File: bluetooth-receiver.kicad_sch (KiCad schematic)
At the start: 12 parts, among them J1 Barrel_Jack_Switch, J2 AudioJack3_Switch, J3 RCJ-22, SW1 PAUSE, SW2 NEXT, SW3 PREV, SW4 ON_OFF, U1 m18, U2 dd1718pa

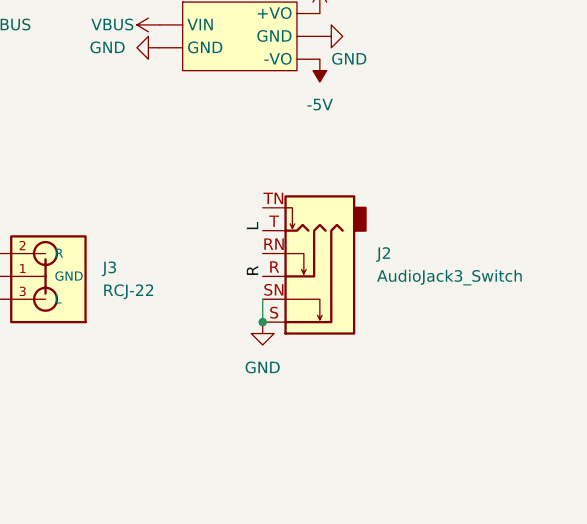
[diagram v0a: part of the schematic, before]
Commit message: Update bluetooth receiver
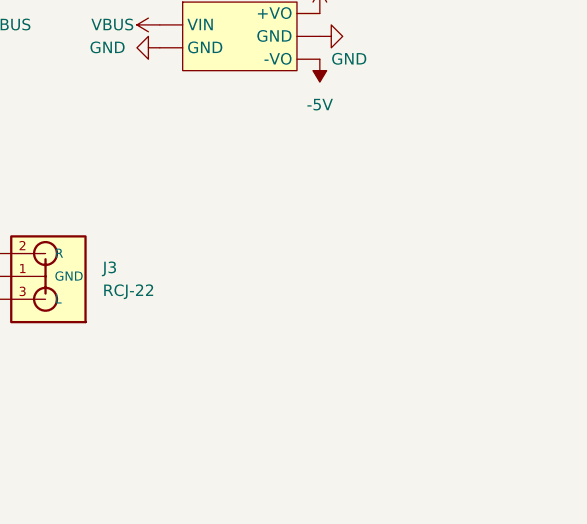
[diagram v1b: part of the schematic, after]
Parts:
- removed J2: AudioJack3_Switch, Connector_Audio:Jack_6.35mm_Neutrik_NMJ6HFD2-AU_Horizontal, symbol Connector:AudioJack3_Switch
- R1, R2, R3: footprint Resistor_THT:R_Axial_DIN0207_L6.3mm_D2.5mm_P10.16mm_Horizontal -> Resistor_THT:R_Axial_DIN0411_L9.9mm_D3.6mm_P5.08mm_Vertical
- SW1, SW2, SW3, SW4: footprint (none) -> pts636:pts636
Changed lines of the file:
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@@
   (junction (at 116.84 123.19) (diameter 0) (color 0 0 0 0)
   )
-  (junction (at 175.26 109.22) (diameter 0) (color 0 0 0 0)
-  )
   (junction (at 104.14 105.41) (diameter 0) (color 0 0 0 0)
   )
@@
     (stroke (width 0) (type default) (color 0 0 0 0))
   )
-  (wire (pts (xy 175.26 106.68) (xy 175.26 109.22))
-    (stroke (width 0) (type default) (color 0 0 0 0))
-  )
   (wire (pts (xy 104.14 105.41) (xy 110.49 105.41))
     (stroke (width 0) (type default) (color 0 0 0 0))
@@
   (wire (pts (xy 146.05 100.33) (xy 143.51 100.33))
     (stroke (width 0) (type default) (color 0 0 0 0))
-  )
-  (label "R" (at 175.26 104.14 90)
-    (effects (font (size 1.27 1.27)) (justify left bottom))
   )
   (label "R" (at 143.51 100.33 0)
     (effects (font (size 1.27 1.27)) (justify left bottom))
   )
-  (label "L" (at 175.26 99.06 90)
-    (effects (font (size 1.27 1.27)) (justify left bottom))
-  )
   (label "L" (at 144.78 107.95 180)
     (effects (font (size 1.27 1.27)) (justify right bottom))
@@
       (effects (font (size 1.016 1.016)) (justify right))
     )
-    (property "Footprint" "" (id 2) (at 111.76 110.49 0)
+    (property "Footprint" "pts636:pts636" (id 2) (at 111.76 110.49 0)
       (effects (font (size 1.27 1.27)) hide)
     )
@@
     )
     (pin "1")
-  )
-  (symbol (lib_id "Connector:AudioJack3_Switch") (at 180.34 104.14 180) (unit 1)
-    (in_bom yes) (on_board yes) (fields_autoplaced)
-    (property "Reference" "J2" (id 0) (at 187.96 101.5999 0)
-      (effects (font (size 1.27 1.27)) (justify right))
-    )
-    (property "Value" "AudioJack3_Switch" (id 1) (at 187.96 104.1399 0)
-      (effects (font (size 1.27 1.27)) (justify right))
-    )
-    (property "Footprint" "Connector_Audio:Jack_6.35mm_Neutrik_NMJ6HFD2-AU_Horizontal" (id 2) (at 180.34 104.14 0)
-      (effects (font (size 1.27 1.27)) hide)
-    )
-    (property "Datasheet" "~" (id 3) (at 180.34 104.14 0)
-      (effects (font (size 1.27 1.27)) hide)
-    )
-    (pin "R")
-    (pin "RN")
-    (pin "S")
-    (pin "SN")
-    (pin "T")
-    (pin "TN")
   )
   (symbol (lib_id "dd1718pa:dd1718pa") (at 172.72 77.47 0) (unit 1)
@@
     (pin "5")
   )
-  (symbol (lib_id "power:GND") (at 175.26 109.22 0) (unit 1)
-    (in_bom yes) (on_board yes) (fields_autoplaced)
-    (property "Reference" "#PWR0102" (id 0) (at 175.26 115.57 0)
-      (effects (font (size 1.27 1.27)) hide)
-    )
-    (property "Value" "GND" (id 1) (at 175.26 114.3 0))
-    (property "Footprint" "" (id 2) (at 175.26 109.22 0)
-      (effects (font (size 1.27 1.27)) hide)
-    )
-    (property "Datasheet" "" (id 3) (at 175.26 109.22 0)
-      (effects (font (size 1.27 1.27)) hide)
-    )
-    (pin "1")
-  )
   (symbol (lib_id "Device:R") (at 110.49 119.38 0) (unit 1)
     (in_bom yes) (on_board yes)
@@
       (effects (font (size 1.27 1.27)) (justify left))
     )
-    (property "Footprint" "Resistor_THT:R_Axial_DIN0207_L6.3mm_D2.5mm_P10.16mm_Horizontal" (id 2) (at 108.712 119.38 90)
+    (property "Footprint" "Resistor_THT:R_Axial_DIN0411_L9.9mm_D3.6mm_P5.08mm_Vertical" (id 2) (at 108.712 119.38 90)
       (effects (font (size 1.27 1.27)) hide)
     )
@@
       (effects (font (size 1.27 1.27)) (justify left))
     )
-    (property "Footprint" "Resistor_THT:R_Axial_DIN0207_L6.3mm_D2.5mm_P10.16mm_Horizontal" (id 2) (at 102.362 119.38 90)
+    (property "Footprint" "Resistor_THT:R_Axial_DIN0411_L9.9mm_D3.6mm_P5.08mm_Vertical" (id 2) (at 102.362 119.38 90)
       (effects (font (size 1.27 1.27)) hide)
     )
@@
       (effects (font (size 1.016 1.016)) (justify right))
     )
-    (property "Footprint" "" (id 2) (at 99.06 110.49 0)
+    (property "Footprint" "pts636:pts636" (id 2) (at 99.06 110.49 0)
       (effects (font (size 1.27 1.27)) hide)
     )
@@
       (effects (font (size 1.27 1.27)) (justify left))
     )
-    (property "Footprint" "Resistor_THT:R_Axial_DIN0207_L6.3mm_D2.5mm_P10.16mm_Horizontal" (id 2) (at 94.742 119.38 90)
+    (property "Footprint" "Resistor_THT:R_Axial_DIN0411_L9.9mm_D3.6mm_P5.08mm_Vertical" (id 2) (at 94.742 119.38 90)
       (effects (font (size 1.27 1.27)) hide)
     )
@@
       (effects (font (size 1.016 1.016)) (justify right))
     )
-    (property "Footprint" "" (id 2) (at 91.44 110.49 0)
+    (property "Footprint" "pts636:pts636" (id 2) (at 91.44 110.49 0)
       (effects (font (size 1.27 1.27)) hide)
     )
@@
       (effects (font (size 1.016 1.016)) (justify right))
     )
-    (property "Footprint" "" (id 2) (at 105.41 110.49 0)
+    (property "Footprint" "pts636:pts636" (id 2) (at 105.41 110.49 0)
       (effects (font (size 1.27 1.27)) hide)
     )
@@
       (reference "#PWR0101") (unit 1) (value "GND") (footprint "")
     )
-    (path "/6b79f7ca-0463-4ae2-a376-906486480987"
-      (reference "#PWR0102") (unit 1) (value "GND") (footprint "")
-    )
     (path "/0d7bed1d-044a-404d-a28c-3617efc84a2e"
       (reference "#PWR0103") (unit 1) (value "GND") (footprint "")
@@
       (reference "J1") (unit 1) (value "Barrel_Jack_Switch") (footprint "Connector_BarrelJack:BarrelJack_GCT_DCJ200-10-A_Horizontal")
     )
-    (path "/5ec5e440-51b8-4920-9405-d52c7c07f4f3"
-      (reference "J2") (unit 1) (value "AudioJack3_Switch") (footprint "Connector_Audio:Jack_6.35mm_Neutrik_NMJ6HFD2-AU_Horizontal")
-    )
     (path "/78cb3361-0a6b-4e19-8422-e995eb292f7c"
       (reference "J3") (unit 1) (value "RCJ-22") (footprint "rcj-22:rcj-22")
     )
     (path "/a0d5fcce-0d78-4065-8ea8-61a7491aebce"
-      (reference "R1") (unit 1) (value "51k") (footprint "Resistor_THT:R_Axial_DIN0207_L6.3mm_D2.5mm_P10.16mm_Horizontal")
+      (reference "R1") (unit 1) (value "51k") (footprint "Resistor_THT:R_Axial_DIN0411_L9.9mm_D3.6mm_P5.08mm_Vertical")
     )
     (path "/79c88f4e-2037-4e51-a10c-d45e7756ae36"
-      (reference "R2") (unit 1) (value "33k") (footprint "Resistor_THT:R_Axial_DIN0207_L6.3mm_D2.5mm_P10.16mm_Horizontal")
+      (reference "R2") (unit 1) (value "33k") (footprint "Resistor_THT:R_Axial_DIN0411_L9.9mm_D3.6mm_P5.08mm_Vertical")
     )
     (path "/6e8600ba-7a15-4837-ad0e-bec5f75606b5"
-      (reference "R3") (unit 1) (value "9k1") (footprint "Resistor_THT:R_Axial_DIN0207_L6.3mm_D2.5mm_P10.16mm_Horizontal")
+      (reference "R3") (unit 1) (value "9k1") (footprint "Resistor_THT:R_Axial_DIN0411_L9.9mm_D3.6mm_P5.08mm_Vertical")
     )
     (path "/bd18efbb-c736-4462-bc80-932b66490474"
-      (reference "SW1") (unit 1) (value "PAUSE") (footprint "")
+      (reference "SW1") (unit 1) (value "PAUSE") (footprint "pts636:pts636")
     )
     (path "/9051a7d2-a3c0-4edf-96c9-aa82b1fced31"
-      (reference "SW2") (unit 1) (value "NEXT") (footprint "")
+      (reference "SW2") (unit 1) (value "NEXT") (footprint "pts636:pts636")
     )
     (path "/f3e2b11d-419a-4fa3-bcc0-f22e190a8162"
-      (reference "SW3") (unit 1) (value "PREV") (footprint "")
+      (reference "SW3") (unit 1) (value "PREV") (footprint "pts636:pts636")
     )
     (path "/49de3e1a-7e19-4f4a-a255-54d063971da6"
-      (reference "SW4") (unit 1) (value "ON_OFF") (footprint "")
+      (reference "SW4") (unit 1) (value "ON_OFF") (footprint "pts636:pts636")
     )
     (path "/7f41a72a-4dde-4975-921c-e378ac194c7c"

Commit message: Prepare for milling
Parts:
- added J2: Power, Connector_PinHeader_2.54mm:PinHeader_1x02_P2.54mm_Vertical, symbol Connector_Generic:Conn_01x02
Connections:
- net VBUS: now also J2.2 (Pin_2)
- net at J1.3: now also J2.1 (Pin_1)
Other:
- moved on the sheet: J1

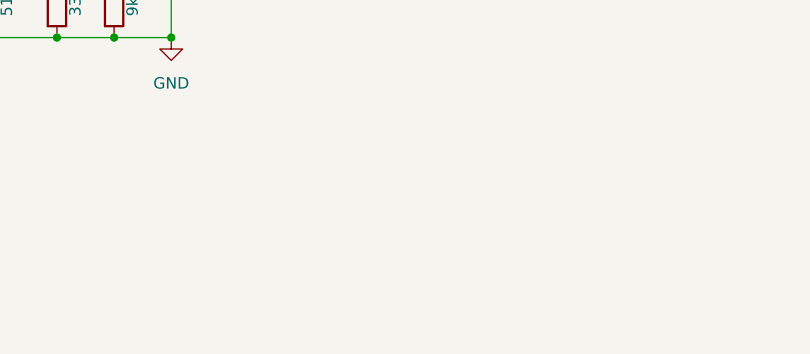
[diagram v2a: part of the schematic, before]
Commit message: Add mounting holes
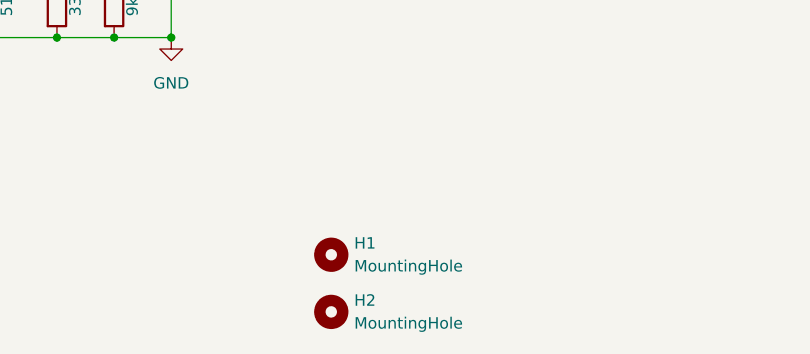
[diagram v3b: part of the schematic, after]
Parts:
- added H1, H2: MountingHole, MountingHole:MountingHole_3.2mm_M3, symbol Mechanical:MountingHole
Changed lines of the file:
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@@
+    )
+  )
+  (symbol (lib_id "Mechanical:MountingHole") (at 134.62 153.67 0) (unit 1)
+    (in_bom yes) (on_board yes) (dnp no) (fields_autoplaced)
+    (property "Reference" "H2" (at 137.16 152.4 0)
+      (effects (font (size 1.27 1.27)) (justify left))
+    )
+    (property "Value" "MountingHole" (at 137.16 154.94 0)
+      (effects (font (size 1.27 1.27)) (justify left))
+    )
+    (property "Footprint" "MountingHole:MountingHole_3.2mm_M3" (at 134.62 153.67 0)
+      (effects (font (size 1.27 1.27)) hide)
+    )
+    (property "Datasheet" "~" (at 134.62 153.67 0)
+      (effects (font (size 1.27 1.27)) hide)
+    )
+    (instances
+      (project "bluetooth-receiver"
+        (path "/c0ba571a-c483-4088-a1a0-d3377704368f"
+          (reference "H2") (unit 1)
+        )
+      )
     )
   )
@@
         )
       )
+    )
+  )
+  (symbol (lib_id "Mechanical:MountingHole") (at 134.62 147.32 0) (unit 1)
+    (in_bom yes) (on_board yes) (dnp no) (fields_autoplaced)
+    (property "Reference" "H1" (at 137.16 146.05 0)
+      (effects (font (size 1.27 1.27)) (justify left))
+    )
+    (property "Value" "MountingHole" (at 137.16 148.59 0)
+      (effects (font (size 1.27 1.27)) (justify left))
+    )
+    (property "Footprint" "MountingHole:MountingHole_3.2mm_M3" (at 134.62 147.32 0)
+      (effects (font (size 1.27 1.27)) hide)
+    )
+    (property "Datasheet" "~" (at 134.62 147.32 0)
+      (effects (font (size 1.27 1.27)) hide)
+    )
+    (instances
+      (project "bluetooth-receiver"
+        (path "/c0ba571a-c483-4088-a1a0-d3377704368f"
+          (reference "H1") (unit 1)
+        )
+      )
